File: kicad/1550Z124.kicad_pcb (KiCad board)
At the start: 2 copper layers, 213.3 x 137.3 mm, 146 parts, among them J1 Conn_02x07_Odd_Even, J2 Conn_01x02, K1 Fujitsu_FTR-K1C, K10 Fujitsu_FTR-K1C, K11 Fujitsu_FTR-K1C, K12 Fujitsu_FTR-K1C, K13 Fujitsu_FTR-K1C, K14 Fujitsu_FTR-K1C, K15 Fujitsu_FTR-K1C, K16 Fujitsu_FTR-K1C, K17 Fujitsu_FTR-K1C, K18 Fujitsu_FTR-K1C, K2 Fujitsu_FTR-K1C, K3 Fujitsu_FTR-K1C, K4 Fujitsu_FTR-K1C, K5 Fujitsu_FTR-K1C, K6 Fujitsu_FTR-K1C, K7 Fujitsu_FTR-K1C, K8 Fujitsu_FTR-K1C, K9 Fujitsu_FTR-K1C, Q1 BC817, Q10 BC817, Q11 BC817, Q12 BC817, Q2 BC817, Q3 BC817, Q4 BC817, Q5 BC817, Q6 BC817, Q7 BC817, Q8 BC817, Q9 BC817

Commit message: Some more layout
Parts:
- TRX1, TRX2: moved to B.Cu
- moved J1 216.0 mm to (159.4, 185.4), turned to 90 degrees
- moved C7 211.1 mm to (144.8, 197.1)
- moved C8 211.1 mm to (145.6, 183.8)
- moved D23 211.1 mm to (139.7, 197.7)
- moved D30 211.1 mm to (147.6, 193.2)
- moved J2 211.1 mm to (134.1, 183.6)
- moved R21 211.1 mm to (141.0, 191.6)
- moved F1 211.1 mm to (133.5, 190.8)
- moved L1 186.8 mm to (191.1, 179.7)
- moved L2 184.2 mm to (186.1, 99.1)
- moved E8 182.1 mm to (211.5, 96.5), turned to 45 degrees
- moved TRX2 171.0 mm to (207.0, 101.0), turned to 90 degrees
- moved TRX1 155.4 mm to (207.0, 164.5), turned to 270 degrees
- moved E7 154.8 mm to (211.5, 168.9), turned to 315 degrees
- moved E2 5.55 mm to (231.1, 126.4), turned to 45 degrees
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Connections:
- E7 pad 1: RADIO_1 -> Net-(E7-Pad1)
- E8 pad 1: RADIO_2 -> Net-(E8-Pad1)
- L1 pad 2: Net-(L1-Pad2) -> Net-(E7-Pad1)
- L2 pad 2: Net-(L2-Pad2) -> Net-(E8-Pad1)
- TRX1 pad 1: Net-(L1-Pad2) -> Net-(E7-Pad1)
- TRX2 pad 1: Net-(L2-Pad2) -> Net-(E8-Pad1)
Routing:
- net +12V: track 24.1 -> 96.2 mm
- net GND: track 49.0 -> 120.3 mm, vias 4 -> 14
- net RADIO_2: track 7.50 -> 45.0 mm
- net RADIO_1: track 7.50 -> 45.0 mm
- net Net-(K14-Pad2): track 0.00 -> 36.0 mm
- net Net-(K10-Pad3): track 0.00 -> 35.9 mm
- net Net-(K1-Pad2): track 0.00 -> 35.9 mm
- net Net-(K13-Pad2): track 0.00 -> 35.8 mm
- net Net-(K2-Pad2): track 0.00 -> 35.8 mm
- net Net-(K15-Pad1): track 0.00 -> 21.6 mm
- net Net-(K4-Pad1): track 0.00 -> 21.6 mm
- net Net-(K10-Pad1): track 0.00 -> 21.4 mm
- net Net-(K3-Pad1): track 0.00 -> 21.4 mm
- net Net-(K16-Pad1): track 0.00 -> 21.4 mm
- net Net-(A4-Pad1): track 0.00 -> 19.7 mm
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
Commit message: Some more layout
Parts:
- moved C7 121.8 mm to (129.5, 76.2)
- moved R21 120.4 mm to (128.5, 71.8)
- moved F1 119.0 mm to (134.4, 71.8)
- moved D23 116.2 mm to (129.2, 81.9)
- moved D30 115.2 mm to (129.3, 79.4)
- moved C8 104.8 mm to (146.9, 79.0)
- moved J2 104.8 mm to (135.3, 78.8)
- moved L2 14.9 mm to (191.1, 85.1)
- moved J1 8.91 mm to (158.8, 194.3)
- moved R26 3.11 mm to (197.6, 167.9)
- moved D31 3.07 mm to (200.2, 168.2)
- moved Q9 1.21 mm to (200.5, 164.1)
- moved R1 0.90 mm to (130.8, 168.0)
- moved C11 0.67 mm to (196.6, 165.0)
- moved D1 0.63 mm to (133.3, 167.9)
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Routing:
- net RADIO_1: track 45.0 -> 360.3 mm
- net RADIO_2: track 45.0 -> 354.4 mm
- net +12V: track 96.2 -> 211.3 mm
- net Net-(D13-Pad2): track 9.43 -> 58.8 mm, vias 0 -> 1
- net GND: track 120.3 -> 162.7 mm, vias 14 -> 22
- net Net-(E8-Pad1): track 3.59 -> 19.7 mm
- net Net-(E7-Pad1): track 3.59 -> 19.1 mm
- net Net-(D33-Pad2): track 6.28 -> 11.3 mm
- net Net-(D4-Pad2): track 6.28 -> 10.8 mm
- net Net-(D34-Pad2): track 6.28 -> 10.8 mm
- net Net-(D18-Pad2): track 6.28 -> 10.8 mm
- net Net-(D3-Pad2): track 6.50 -> 11.0 mm
- net Net-(C12-Pad1): track 0.00 -> 4.45 mm
- net Net-(C3-Pad1): track 0.00 -> 4.41 mm
- net Net-(C6-Pad1): track 0.00 -> 4.33 mm
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- added copper zone on B.Cu, net GND

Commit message: Some layout and routing
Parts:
- D13, D14, D17, D18, D28, D29, D3, D33, D34, D4, D43, D44: moved to F.Cu
- moved J1 114.8 mm to (272.4, 178.4)
- moved R21 18.6 mm to (131.1, 90.2)
- moved D30 18.6 mm to (131.8, 97.8)
- moved F1 18.6 mm to (136.9, 90.2)
- moved C7 18.6 mm to (132.1, 94.6)
- moved C8 18.6 mm to (149.4, 97.4)
- moved D23 18.6 mm to (131.7, 100.3)
- moved J2 18.6 mm to (137.9, 97.2)
- moved L1 18.2 mm to (182.2, 163.8), turned to 270 degrees
- moved L2 16.7 mm to (186.1, 101.0)
- moved C1 13.1 mm to (141.0, 165.1), turned to 0 degrees
- moved C5 12.7 mm to (175.7, 165.4), turned to 0 degrees
- moved R5 8.66 mm to (113.0, 165.1), turned to 180 degrees
- moved R17 8.66 mm to (148.0, 165.1), turned to 180 degrees
- moved R1 6.64 mm to (136.8, 165.1), turned to 180 degrees
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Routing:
- net +12V: track 211.3 -> 556.9 mm, vias 0 -> 1
- net RADIO_1: track 360.3 -> 227.7 mm
- net RADIO_2: track 354.4 -> 232.1 mm
- net Net-(D36-Pad2): track 8.99 -> 59.2 mm, vias 0 -> 1
- net Net-(D14-Pad2): track 8.99 -> 59.1 mm, vias 0 -> 1
- net Net-(D20-Pad2): track 9.21 -> 59.1 mm, vias 0 -> 1
- net Net-(D35-Pad2): track 9.21 -> 58.9 mm, vias 0 -> 1
- net GND: track 162.7 -> 188.2 mm, vias 22 -> 44
- net Net-(E7-Pad1): track 19.1 -> 40.9 mm
- net Net-(E8-Pad1): track 19.7 -> 9.31 mm
- net Net-(C4-Pad1): track 0.00 -> 5.02 mm
- net Net-(C10-Pad1): track 0.00 -> 5.02 mm
- net Net-(C14-Pad1): track 0.00 -> 4.75 mm
- net Net-(C13-Pad1): track 0.00 -> 4.75 mm
- net A4R2: track 0.00 -> 2.31 mm
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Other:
- board size 213.3 x 137.3 mm -> 213.5 x 137.3 mm
- board text added: "6x2 Antenna Switch"
- board text added: "http://sq9nje.pl http://quirky.solutions"

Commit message: routing finished
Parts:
- added REF**: MountingHole_3.2mm_M3_ISO7380_Pad, MountingHole:MountingHole_3.2mm_M3_ISO7380_Pad, F.Cu at (305.0, 172.5)
- added REF**: MountingHole_3.2mm_M3_ISO7380_Pad, MountingHole:MountingHole_3.2mm_M3_ISO7380_Pad, F.Cu at (255.0, 96.4)
- added REF**: MountingHole_3.2mm_M3_ISO7380_Pad, MountingHole:MountingHole_3.2mm_M3_ISO7380_Pad, F.Cu at (305.0, 96.4)
- added REF**: MountingHole_3.2mm_M3_ISO7380_Pad, MountingHole:MountingHole_3.2mm_M3_ISO7380_Pad, F.Cu at (160.8, 172.5)
- added REF**: MountingHole_3.2mm_M3_ISO7380_Pad, MountingHole:MountingHole_3.2mm_M3_ISO7380_Pad, F.Cu at (160.8, 96.4)
- added REF**: MountingHole_3.2mm_M3_ISO7380_Pad, MountingHole:MountingHole_3.2mm_M3_ISO7380_Pad, F.Cu at (110.8, 172.5)
- added REF**: MountingHole_3.2mm_M3_ISO7380_Pad, MountingHole:MountingHole_3.2mm_M3_ISO7380_Pad, F.Cu at (110.8, 96.4)
- L1, L2: footprint Inductor_THT:L_Axial_L13.0mm_D4.5mm_P15.24mm_Horizontal_Fastron_HCCC -> Resistor_THT:R_Axial_DIN0411_L9.9mm_D3.6mm_P12.70mm_Horizontal
- moved R21 161.1 mm to (291.7, 101.6), turned to 180 degrees
- moved D23 155.1 mm to (286.8, 101.6), turned to 180 degrees
- moved J2 149.2 mm to (287.0, 92.7)
- moved D30 146.3 mm to (278.1, 94.2), turned to 90 degrees
- moved C7 144.9 mm to (276.9, 101.6), turned to 90 degrees
- moved F1 144.4 mm to (281.3, 94.0), turned to 270 degrees
- moved C8 117.9 mm to (267.3, 99.7), turned to 90 degrees
- moved R26 32.3 mm to (229.2, 174.4), turned to 90 degrees
- moved D31 32.1 mm to (231.6, 174.4), turned to 270 degrees
- moved C11 31.5 mm to (226.7, 174.4), turned to 90 degrees
- moved Q9 24.9 mm to (223.2, 174.3), turned to 180 degrees
- moved C6 13.5 mm to (280.9, 165.1), turned to 0 degrees
- moved C2 13.1 mm to (245.7, 165.1), turned to 0 degrees
- moved C12 9.62 mm to (311.8, 167.6)
- moved R31 8.66 mm to (287.7, 165.1), turned to 180 degrees
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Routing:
- net A1R2: track 2.31 -> 176.1 mm
- net A1R1: track 2.32 -> 145.7 mm, vias 0 -> 1
- net A2R2: track 2.31 -> 144.4 mm
- net A2R1: track 2.25 -> 123.3 mm, vias 0 -> 2
- net A3R2: track 2.31 -> 113.0 mm
- net A4R2: track 2.31 -> 72.1 mm
- net A3R1: track 2.59 -> 49.8 mm, vias 0 -> 1
- net A4R1: track 2.66 -> 48.1 mm, vias 0 -> 1
- net A6R2: track 2.31 -> 46.5 mm
- net A5R2: track 2.31 -> 39.8 mm
- net Net-(E7-Pad1): track 40.9 -> 8.67 mm
- net A6R1: track 2.66 -> 32.1 mm
- net +12V: track 556.9 -> 577.4 mm
- net Net-(D33-Pad2): track 12.8 -> 31.2 mm
- net GND: track 188.2 -> 202.0 mm, vias 44 -> 59
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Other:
- board size 213.5 x 137.3 mm -> 213.3 x 96 mm

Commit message: top silk
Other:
- board text added: "+"
- board text added: "-"
- board text added: "12V"
- board text added: "A1"
- board text added: "A2"
- board text added: "A3"
- board text added: "A4"
- board text added: "A5"
- board text added: "A6"
- board text added: "G"
- board text added: "RADIO 1"
- board text added: "RADIO 2"
- board text added: "http://sq9nje.pl"
- board text removed: "http://sq9nje.pl http://quirky.solutions"

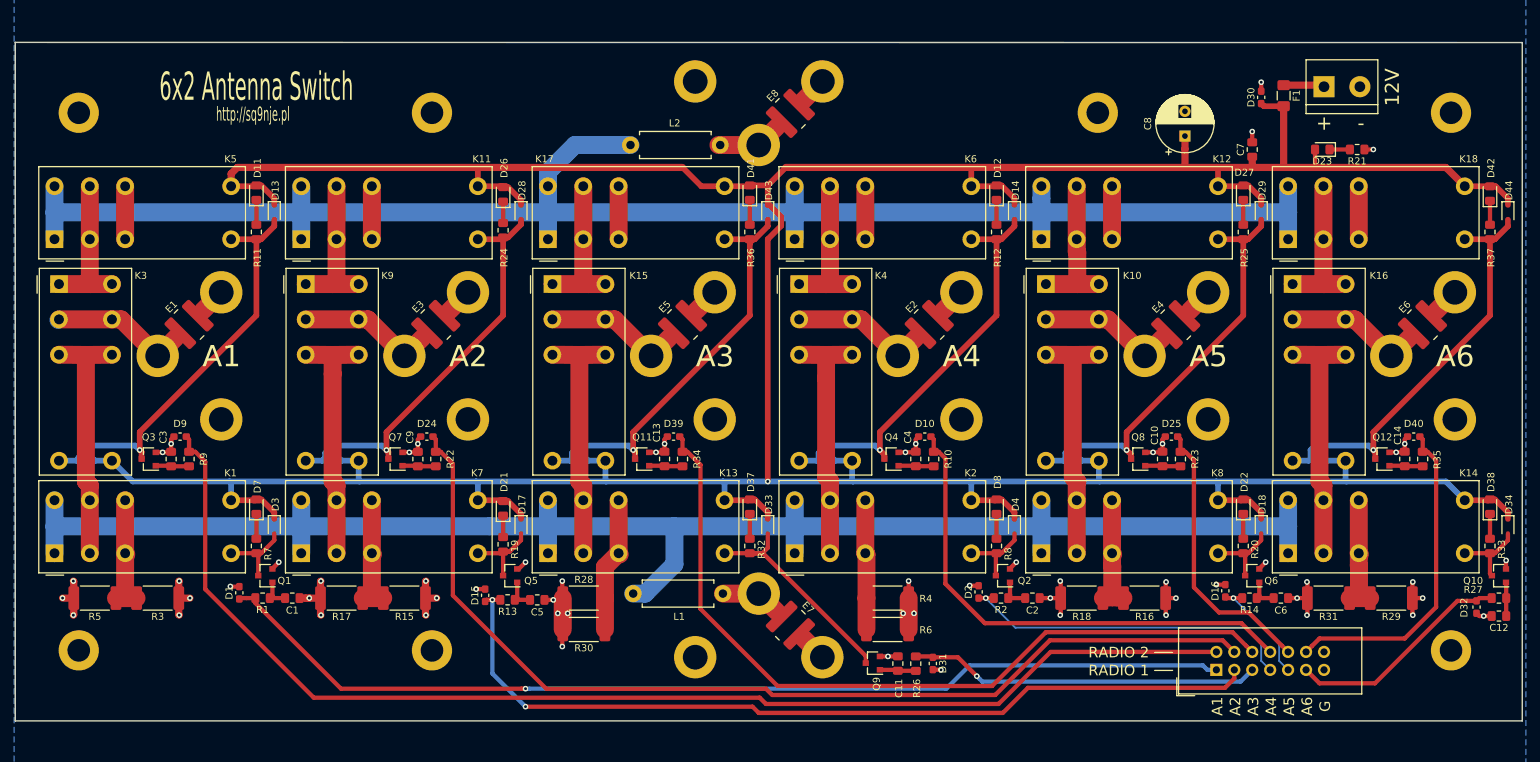
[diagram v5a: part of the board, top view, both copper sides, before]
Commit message: top ground plane
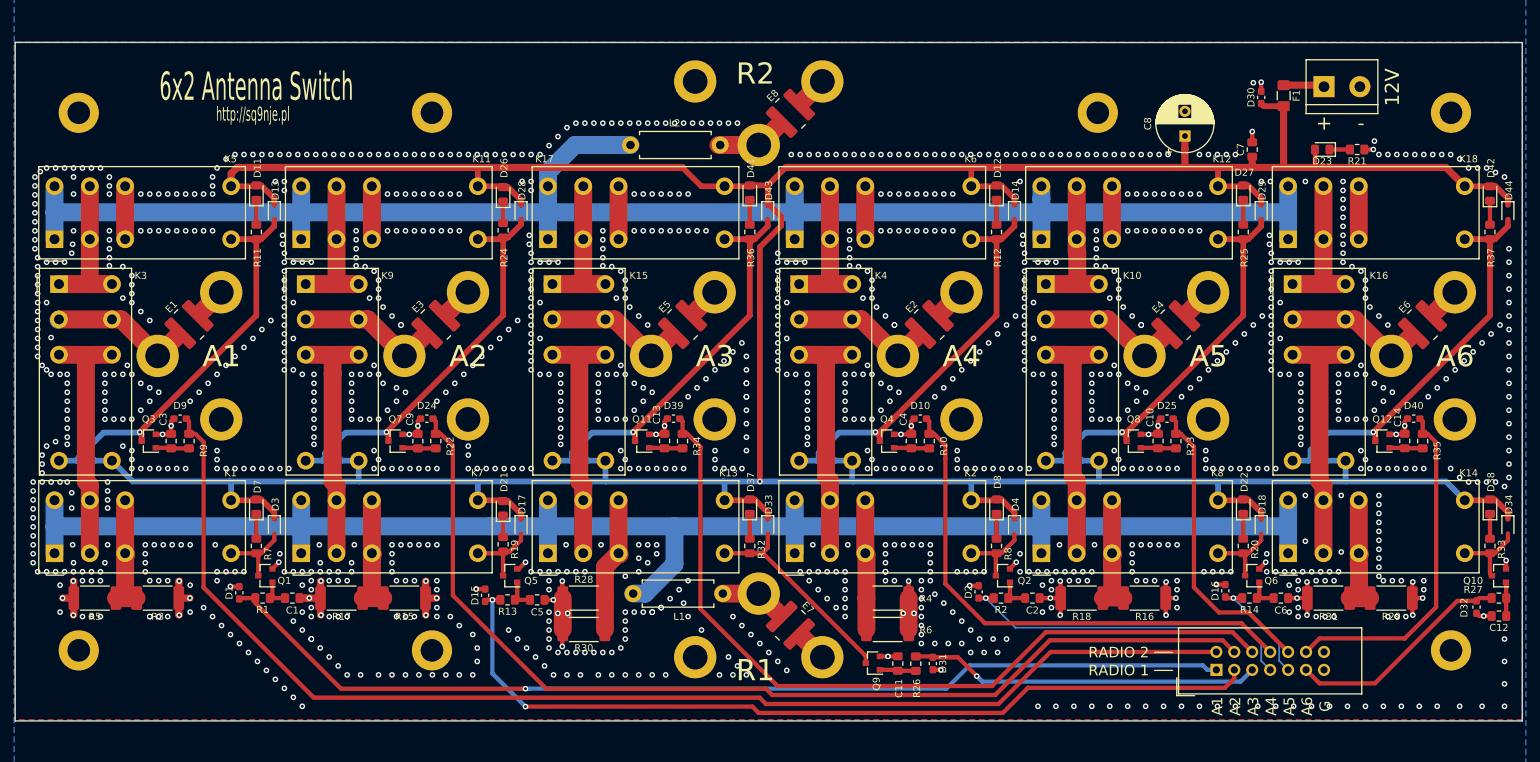
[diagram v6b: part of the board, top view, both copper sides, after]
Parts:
- moved D10 2.62 mm to (229.9, 139.7)
- moved D25 2.62 mm to (264.8, 139.7)
- moved C10 2.62 mm to (263.5, 142.9)
- moved C4 2.62 mm to (228.6, 142.9)
- moved R10 2.62 mm to (231.1, 142.9)
- moved Q4 2.62 mm to (225.2, 142.9)
- moved Q8 2.62 mm to (260.1, 142.9)
- moved R23 2.62 mm to (266.1, 142.9)
- moved C9 2.54 mm to (158.8, 142.9)
- moved D24 2.54 mm to (160.0, 139.7)
- moved D39 2.54 mm to (194.9, 139.7)
- moved D40 2.54 mm to (299.7, 139.7)
- moved D9 2.54 mm to (125.1, 139.7)
- moved C13 2.54 mm to (193.7, 142.9)
- moved C14 2.54 mm to (298.4, 142.9)
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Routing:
- net A5R2: track 39.8 -> 42.6 mm
- net A4R2: track 72.1 -> 74.9 mm
- net A6R2: track 46.5 -> 49.1 mm
- net A2R2: track 144.4 -> 146.9 mm
- net A3R2: track 113.0 -> 115.5 mm
- net A1R2: track 176.1 -> 178.7 mm
- net Net-(D19-Pad2): track 59.0 -> 57.0 mm
- net Net-(D13-Pad2): track 58.6 -> 56.5 mm
- net Net-(D36-Pad2): track 59.2 -> 57.2 mm
- net Net-(D20-Pad2): track 59.1 -> 57.1 mm
- net Net-(D35-Pad2): track 58.9 -> 56.9 mm
- net Net-(D14-Pad2): track 59.1 -> 57.2 mm
- net GND: vias 59 -> 1286
- added copper zone on F.Cu, net GND
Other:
- board text added: "R1"
- board text added: "R2"

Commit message: vias, lots of vias
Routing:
- net GND: track 202.0 -> 203.0 mm, vias 1286 -> 2791
